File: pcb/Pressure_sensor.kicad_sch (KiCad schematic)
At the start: 6 parts, among them J19 Conn_03x01, U8 DPS310XTSA1

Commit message: Polishin pt1
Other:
- note added: "Pressure sensor"
- company: (none) -> Infineon Technologies
- title: (none) -> SensEdu 0.7
- moved on the sheet: C15, R41, R42

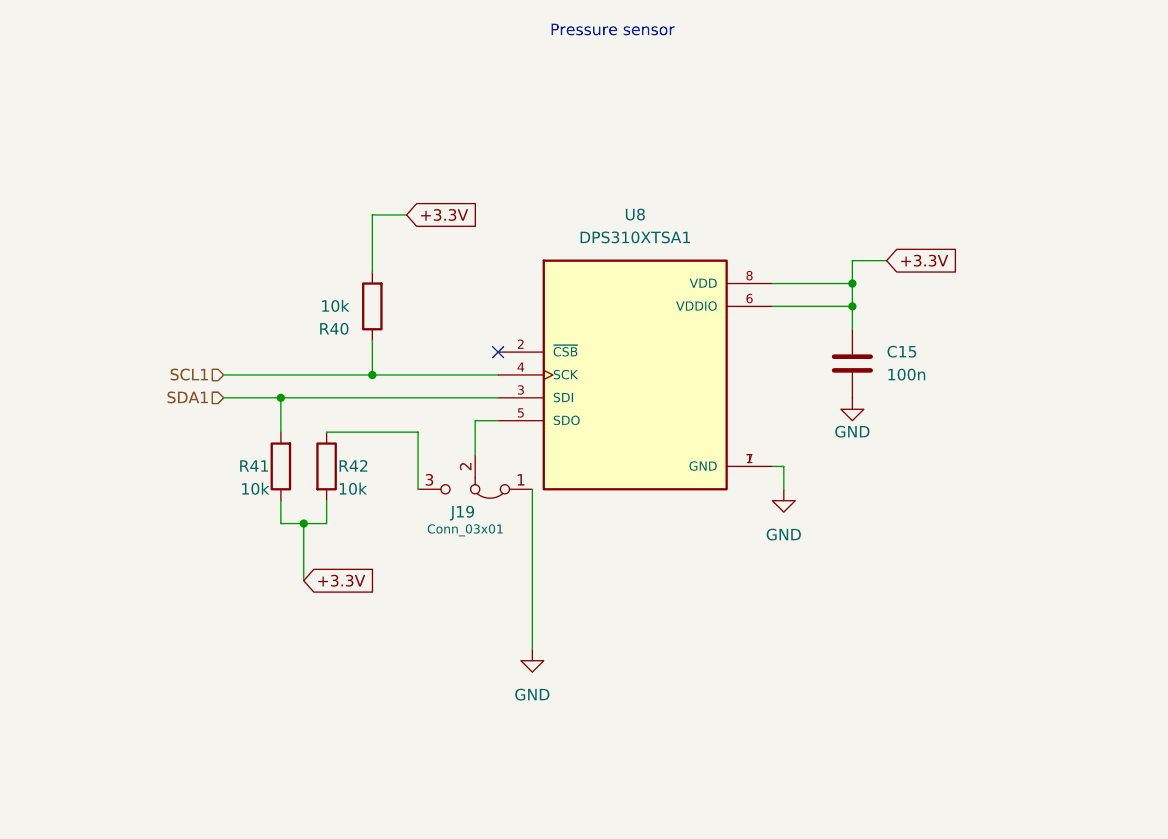
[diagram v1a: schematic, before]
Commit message: Changing Pressure Sensor Sheet
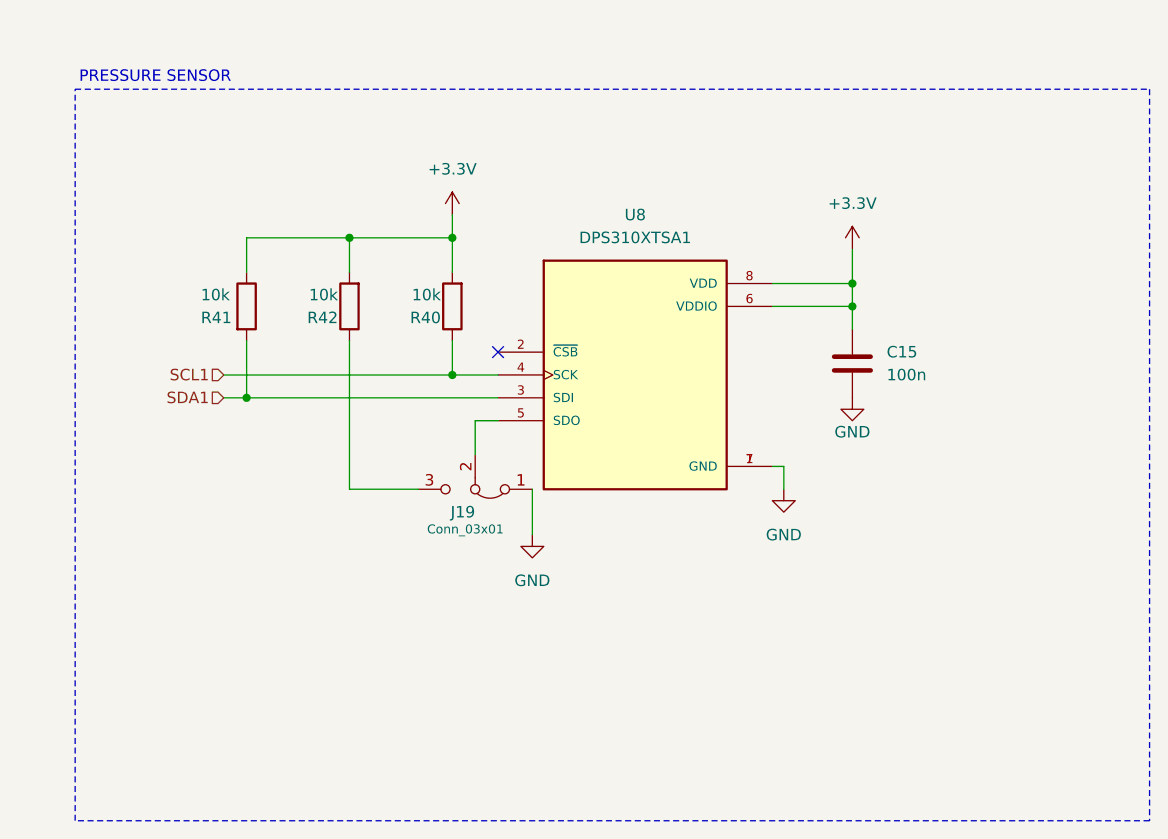
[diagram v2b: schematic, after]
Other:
- note added: "PRESSURE SENSOR"
- note removed: "Pressure sensor"
- moved on the sheet: R40, R41, R42

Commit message: refactor: Edit speaker/mic symbols and polish
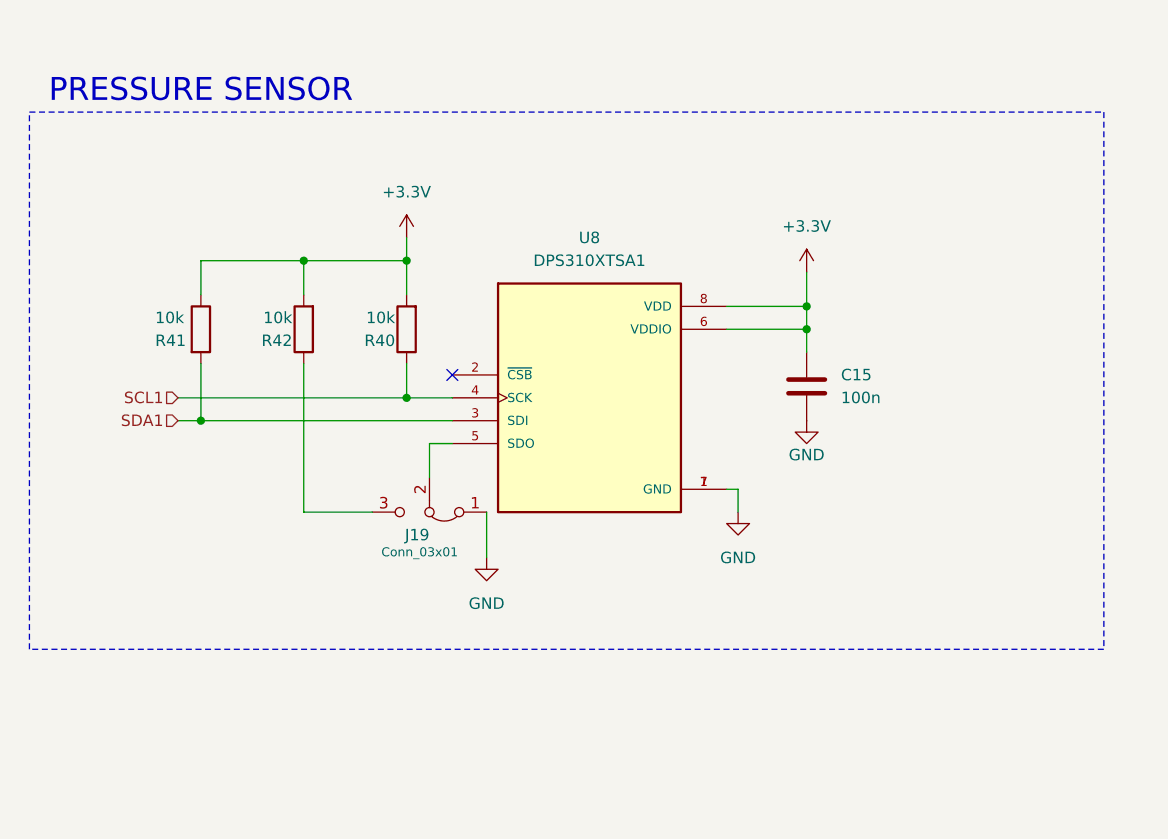
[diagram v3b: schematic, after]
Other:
- moved on the sheet: C15, J19, R40, R41, R42, U8
